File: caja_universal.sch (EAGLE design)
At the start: 39 parts, among them IC1 AD711N, IC2 AD620N, IC3 TL084P, IC4 TL084P, IC5 AD711N

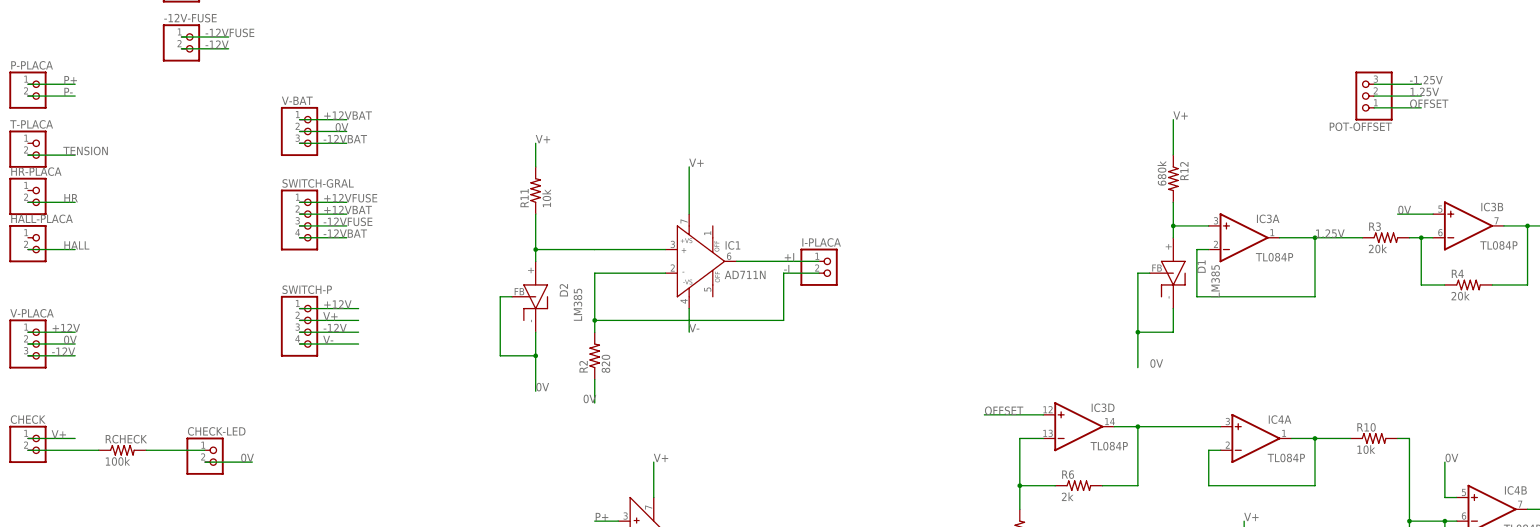
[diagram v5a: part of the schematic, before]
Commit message: Corregimos placa de conexion universal y mochila
Esta version se envia a imprimir
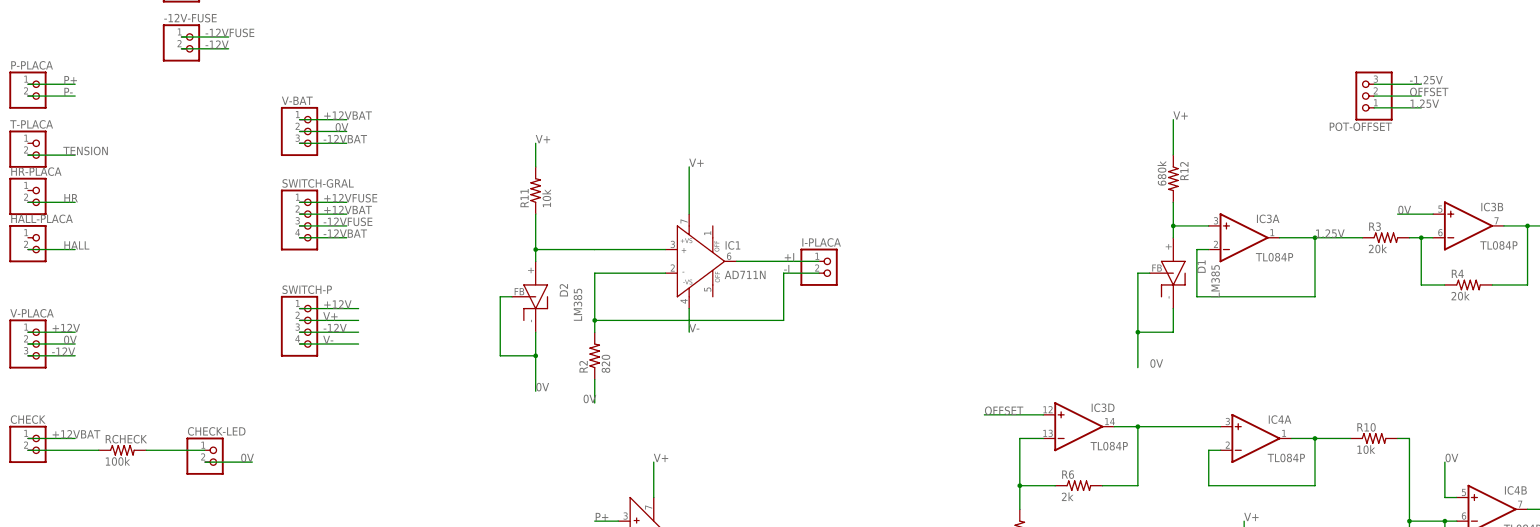
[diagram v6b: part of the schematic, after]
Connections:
- net +12VBAT: now also CHECK.1
- net 1.25V: now also POT-OFFSET.1; no longer POT-OFFSET.2
- net OFFSET: now also POT-OFFSET.2; no longer POT-OFFSET.1
- net V+: no longer CHECK.1
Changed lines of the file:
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@@
 <?xml version="1.0" encoding="utf-8"?>
 <!DOCTYPE eagle SYSTEM "eagle.dtd">
-<eagle version="9.2.2">
+<eagle version="7.7.0">
 <drawing>
 <settings>
 <setting alwaysvectorfont="no"/>
-<setting keepoldvectorfont="yes"/>
 <setting verticaltext="up"/>
 </settings>
@@
 <net name="V+" class="0">
 <segment>
-<pinref part="CHECK" gate="G$1" pin="1"/>
-<wire x1="-38.1" y1="66.04" x2="-27.94" y2="66.04" width="0.1524" layer="91"/>
-<label x="-33.02" y="66.04" size="1.778" layer="95"/>
-</segment>
-<segment>
 <pinref part="IC2" gate="G$1" pin="+V"/>
 <wire x1="96.52" y1="53.34" x2="96.52" y2="60.96" width="0.1524" layer="91"/>
@@
 <wire x1="20.32" y1="114.3" x2="30.48" y2="114.3" width="0.1524" layer="91"/>
 <label x="25.4" y="114.3" size="1.778" layer="95"/>
+</segment>
+<segment>
+<pinref part="CHECK" gate="G$1" pin="1"/>
+<wire x1="-38.1" y1="66.04" x2="-27.94" y2="66.04" width="0.1524" layer="91"/>
+<label x="-33.02" y="66.04" size="1.778" layer="95"/>
 </segment>
 </net>
@@
 </segment>
 <segment>
-<pinref part="POT-OFFSET" gate="A" pin="2"/>
-<wire x1="251.46" y1="139.7" x2="261.62" y2="139.7" width="0.1524" layer="91"/>
-<label x="259.08" y="139.7" size="1.778" layer="95"/>
+<pinref part="POT-OFFSET" gate="A" pin="1"/>
+<wire x1="251.46" y1="137.16" x2="261.62" y2="137.16" width="0.1524" layer="91"/>
+<label x="259.08" y="137.16" size="1.778" layer="95"/>
 </segment>
 </net>
@@
 <net name="OFFSET" class="0">
 <segment>
-<pinref part="POT-OFFSET" gate="A" pin="1"/>
-<wire x1="251.46" y1="137.16" x2="261.62" y2="137.16" width="0.1524" layer="91"/>
-<label x="259.08" y="137.16" size="1.778" layer="95"/>
-</segment>
-<segment>
 <pinref part="IC3" gate="D" pin="+IN"/>
 <wire x1="180.34" y1="71.12" x2="167.64" y2="71.12" width="0.1524" layer="91"/>
 <label x="167.64" y="71.12" size="1.778" layer="95"/>
 </segment>
-</net>
+<segment>
+<pinref part="POT-OFFSET" gate="A" pin="2"/>
+<wire x1="251.46" y1="139.7" x2="261.62" y2="139.7" width="0.1524" layer="91"/>
+<label x="259.08" y="139.7" size="1.778" layer="95"/>
+</segment>
+</net>

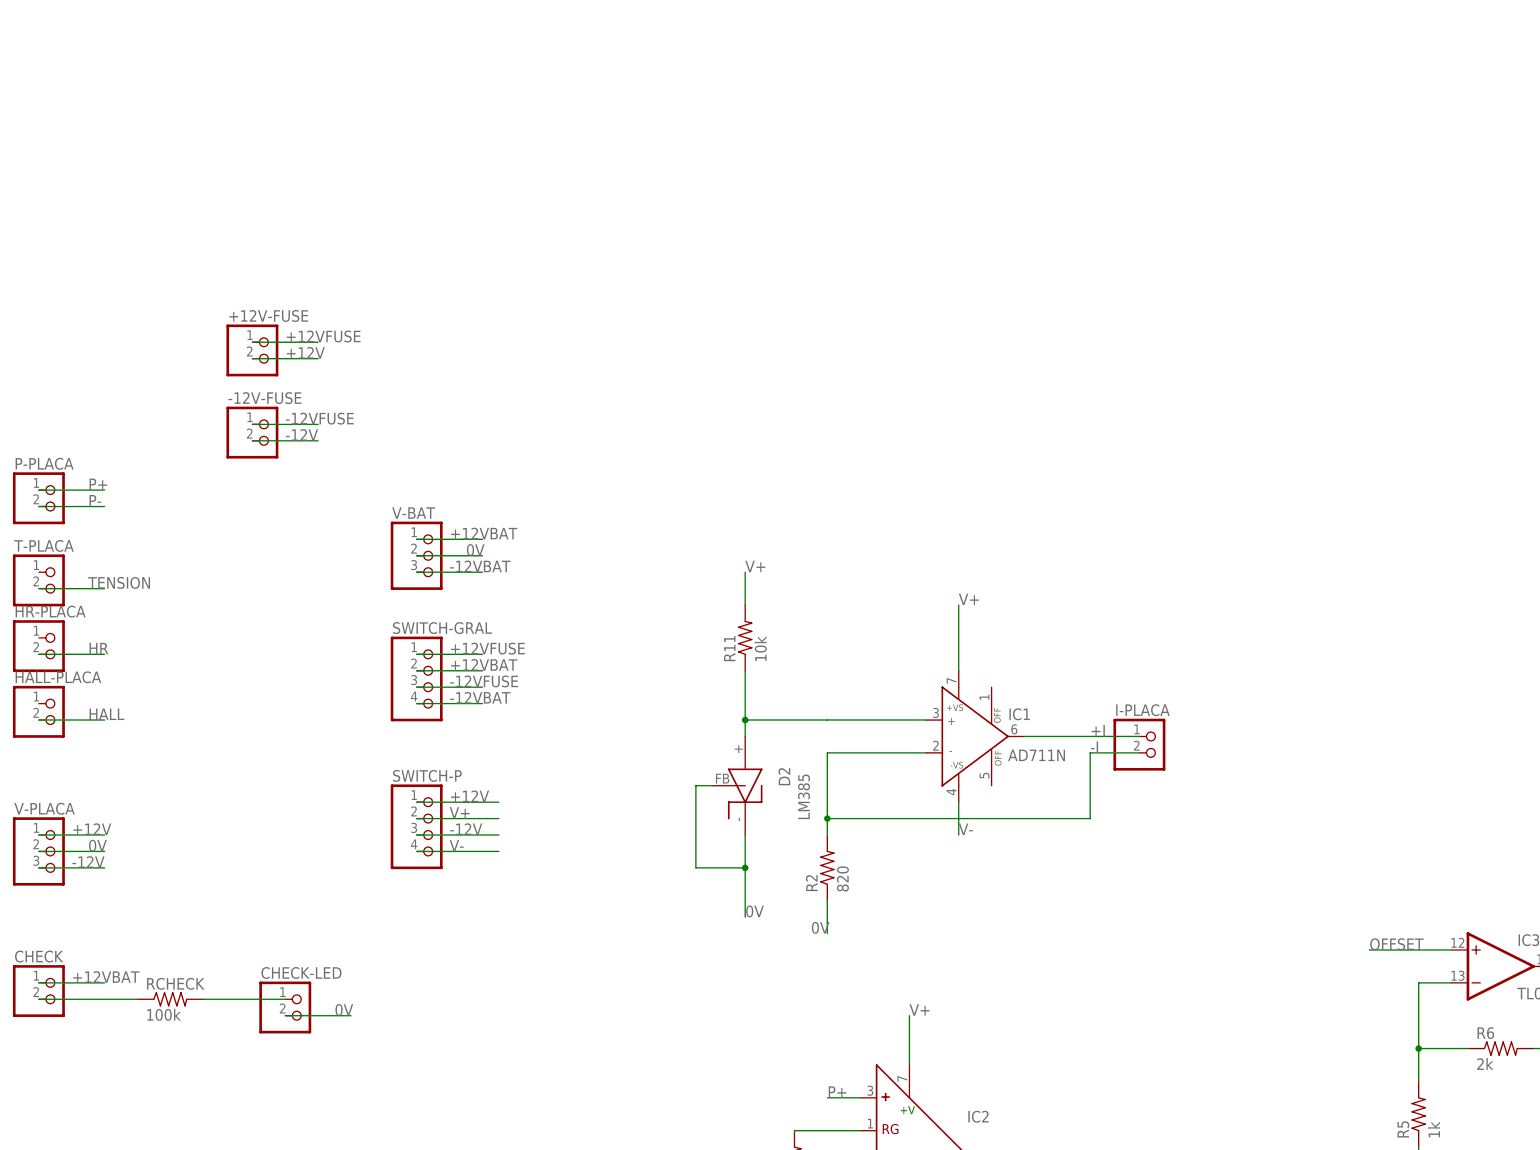
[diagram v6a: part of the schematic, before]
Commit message: Nuevo circuito de sense
Agrego circuito diseñado por Gonza para no tener que usar los cables de check
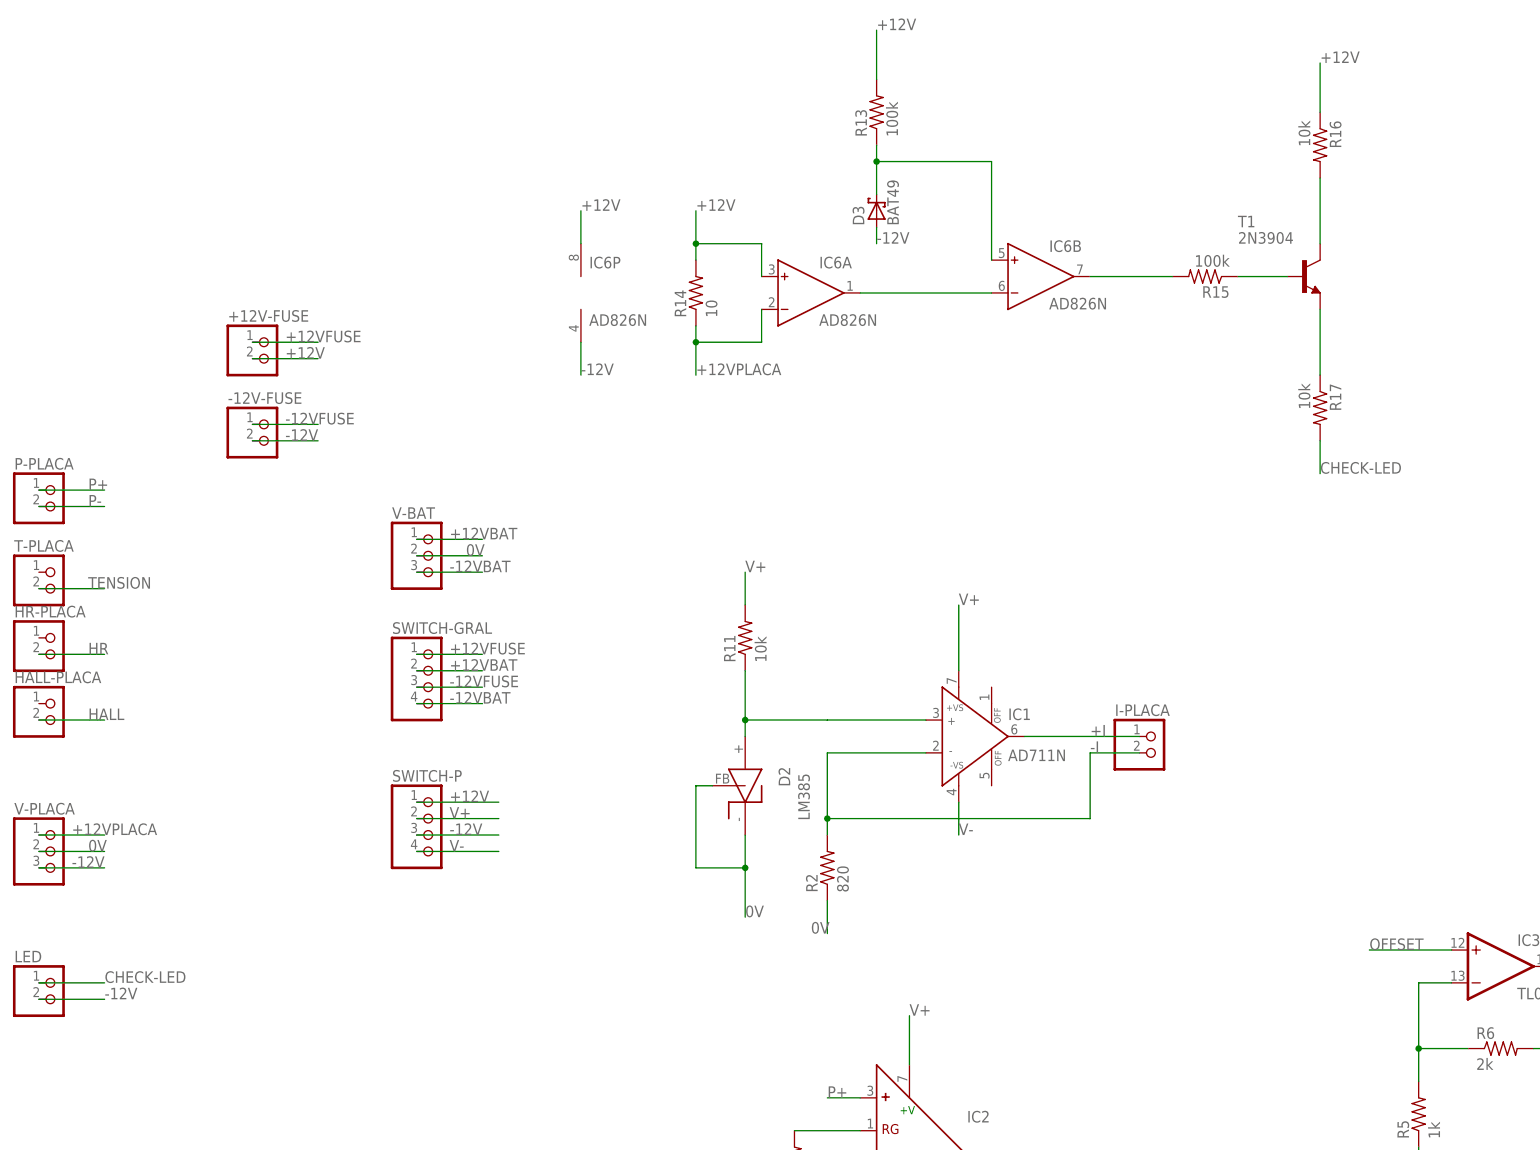
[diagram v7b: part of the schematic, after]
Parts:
- removed CHECK-LED: (no value), pinhead:PINHD-1X2
- removed RCHECK: 100k, resistor:R-US_0204/7
- added D3: BAT49, diode:BAT49
- added IC6: AD826N, analog-devices:AD826N
- added R13, R15: 100k, resistor:R-US_0204/7
- added R14: 10, resistor:R-US_0204/7
- added R16, R17: 10k, resistor:R-US_0204/7
- added T1: 2N3904, transistor:2N3904
- renumbered CHECK to LED
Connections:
- removed net N$1: CHECK-LED.1, RCHECK.2
- removed net N$2: LED.2, RCHECK.1
- new net +12VPLACA: IC6A.IN-, R14.1, V-PLACA.1
- new net CHECK-LED: LED.1, R17.2
- new net N$17: R15.1, T1.B
- new net N$18: R16.2, T1.C
- new net N$19: R17.1, T1.E
- new net N$21: IC6A.OUT, IC6B.IN-
- new net N$23: D3.C, IC6B.IN+, R13.1
- new net N$24: IC6B.OUT, R15.2
- net +12V: now also IC6A.IN+, IC6P.V+, R13.2, R14.2, R16.1; no longer V-PLACA.1
- net +12VBAT: no longer LED.1
- net -12V: now also D3.A, IC6P.V-, LED.2
- net 0V: no longer CHECK-LED.2

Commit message: Version 2.1
Smasheo todo para que los nombres y valores de todos los componentes queden visibles

Cambio los nombres de los integrados para que sean los que usamos
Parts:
- IC1, IC5: value AD711N -> NE5534
- IC6: value AD826N -> TL072
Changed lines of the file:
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@@
 <grid distance="0.1" unitdist="inch" unit="inch" style="lines" multiple="1" display="no" altdistance="0.01" altunitdist="inch" altunit="inch"/>
 <layers>
-<layer number="1" name="Top" color="4" fill="1" visible="no" active="no"/>
-<layer number="16" name="Bottom" color="1" fill="1" visible="no" active="no"/>
-<layer number="17" name="Pads" color="2" fill="1" visible="no" active="no"/>
-<layer number="18" name="Vias" color="2" fill="1" visible="no" active="no"/>
-<layer number="19" name="Unrouted" color="6" fill="1" visible="no" active="no"/>
-<layer number="20" name="Dimension" color="15" fill="1" visible="no" active="no"/>
-<layer number="21" name="tPlace" color="7" fill="1" visible="no" active="no"/>
-<layer number="22" name="bPlace" color="7" fill="1" visible="no" active="no"/>
-<layer number="23" name="tOrigins" color="15" fill="1" visible="no" active="no"/>
-<layer number="24" name="bOrigins" color="15" fill="1" visible="no" active="no"/>
-<layer number="25" name="tNames" color="7" fill="1" visible="no" active="no"/>
-<layer number="26" name="bNames" color="7" fill="1" visible="no" active="no"/>
-<layer number="27" name="tValues" color="7" fill="1" visible="no" active="no"/>
-<layer number="28" name="bValues" color="7" fill="1" visible="no" active="no"/>
+<layer number="1" name="Top" color="4" fill="1" visible="yes" active="no"/>
+<layer number="16" name="Bottom" color="1" fill="1" visible="yes" active="no"/>
+<layer number="17" name="Pads" color="2" fill="1" visible="yes" active="no"/>
+<layer number="18" name="Vias" color="2" fill="1" visible="yes" active="no"/>
+<layer number="19" name="Unrouted" color="6" fill="1" visible="yes" active="no"/>
+<layer number="20" name="Dimension" color="15" fill="1" visible="yes" active="no"/>
+<layer number="21" name="tPlace" color="7" fill="1" visible="yes" active="no"/>
+<layer number="22" name="bPlace" color="7" fill="1" visible="yes" active="no"/>
+<layer number="23" name="tOrigins" color="15" fill="1" visible="yes" active="no"/>
+<layer number="24" name="bOrigins" color="15" fill="1" visible="yes" active="no"/>
+<layer number="25" name="tNames" color="7" fill="1" visible="yes" active="no"/>
+<layer number="26" name="bNames" color="7" fill="1" visible="yes" active="no"/>
+<layer number="27" name="tValues" color="7" fill="1" visible="yes" active="no"/>
+<layer number="28" name="bValues" color="7" fill="1" visible="yes" active="no"/>
 <layer number="29" name="tStop" color="7" fill="3" visible="no" active="no"/>
 <layer number="30" name="bStop" color="7" fill="6" visible="no" active="no"/>
@@
 <layer number="35" name="tGlue" color="7" fill="4" visible="no" active="no"/>
 <layer number="36" name="bGlue" color="7" fill="5" visible="no" active="no"/>
-<layer number="37" name="tTest" color="7" fill="1" visible="no" active="no"/>
-<layer number="38" name="bTest" color="7" fill="1" visible="no" active="no"/>
+<layer number="37" name="tTest" color="7" fill="1" visible="yes" active="no"/>
+<layer number="38" name="bTest" color="7" fill="1" visible="yes" active="no"/>
 <layer number="39" name="tKeepout" color="4" fill="11" visible="no" active="no"/>
 <layer number="40" name="bKeepout" color="1" fill="11" visible="no" active="no"/>
@@
 <layer number="44" name="Drills" color="7" fill="1" visible="no" active="no"/>
 <layer number="45" name="Holes" color="7" fill="1" visible="no" active="no"/>
-<layer number="46" name="Milling" color="3" fill="1" visible="no" active="no"/>
-<layer number="47" name="Measures" color="7" fill="1" visible="no" active="no"/>
-<layer number="48" name="Document" color="7" fill="1" visible="no" active="no"/>
-<layer number="49" name="Reference" color="7" fill="1" visible="no" active="no"/>
-<layer number="51" name="tDocu" color="7" fill="1" visible="no" active="no"/>
-<layer number="52" name="bDocu" color="7" fill="1" visible="no" active="no"/>
+<layer number="46" name="Milling" color="3" fill="1" visible="yes" active="no"/>
+<layer number="47" name="Measures" color="7" fill="1" visible="yes" active="no"/>
+<layer number="48" name="Document" color="7" fill="1" visible="yes" active="no"/>
+<layer number="49" name="Reference" color="7" fill="1" visible="yes" active="no"/>
+<layer number="51" name="tDocu" color="7" fill="1" visible="yes" active="no"/>
+<layer number="52" name="bDocu" color="7" fill="1" visible="yes" active="no"/>
 <layer number="90" name="Modules" color="5" fill="1" visible="yes" active="yes"/>
 <layer number="91" name="Nets" color="2" fill="1" visible="yes" active="yes"/>
@@
 <part name="D1" library="lm385" deviceset="LM385" device=""/>
 <part name="D2" library="lm385" deviceset="LM385" device=""/>
-<part name="IC1" library="analog-devices" deviceset="AD711" device="N"/>
-<part name="IC5" library="analog-devices" deviceset="AD711" device="N"/>
-<part name="IC6" library="analog-devices" deviceset="AD826" device="N"/>
+<part name="IC1" library="analog-devices" deviceset="AD711" device="N" value="NE5534"/>
+<part name="IC5" library="analog-devices" deviceset="AD711" device="N" value="NE5534"/>
+<part name="IC6" library="analog-devices" deviceset="AD826" device="N" value="TL072"/>
 <part name="R13" library="resistor" deviceset="R-US_" device="0204/7" value="100k"/>
 <part name="R14" library="resistor" deviceset="R-US_" device="0204/7" value="10"/>
